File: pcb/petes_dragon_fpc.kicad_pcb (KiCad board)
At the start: 2 copper layers, 154.6 x 140.5 mm, 200 parts

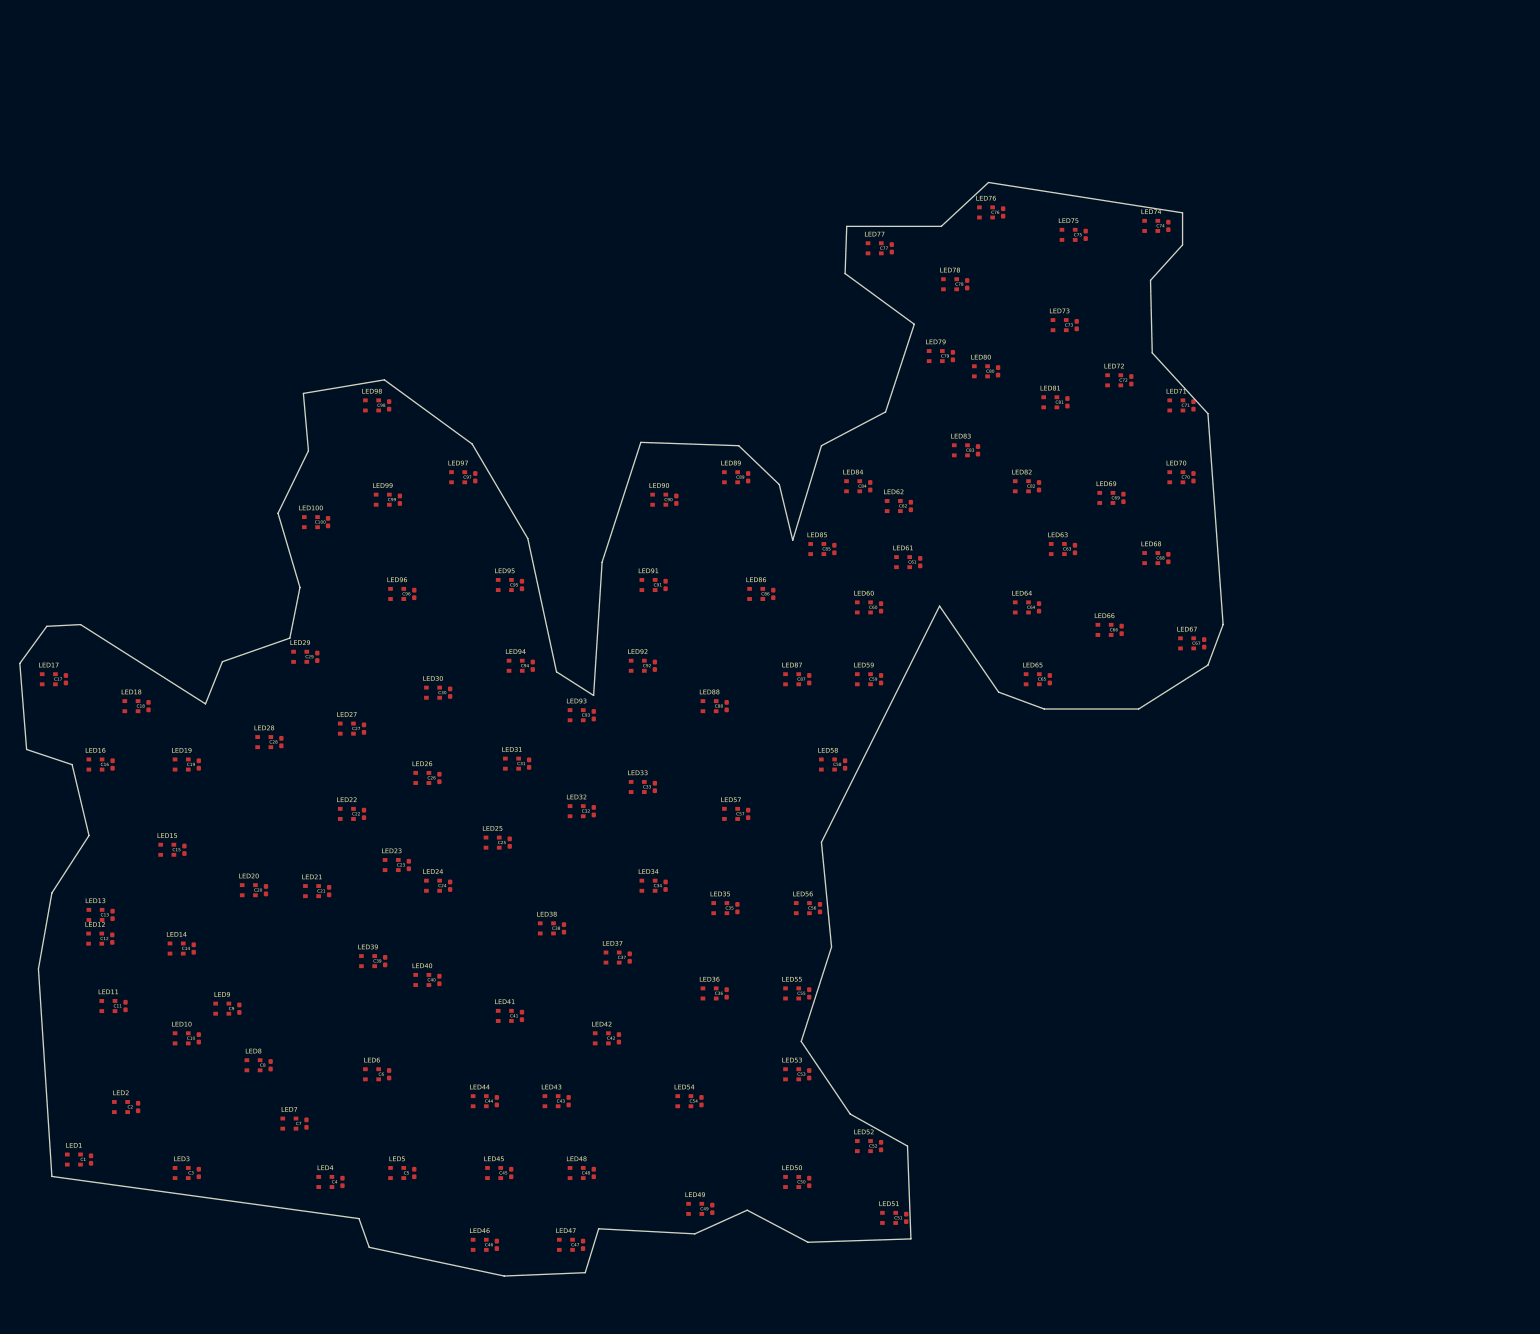
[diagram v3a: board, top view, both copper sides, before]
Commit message: feat(pcb): package KiCad project as zip with tracks for EasyEDA import
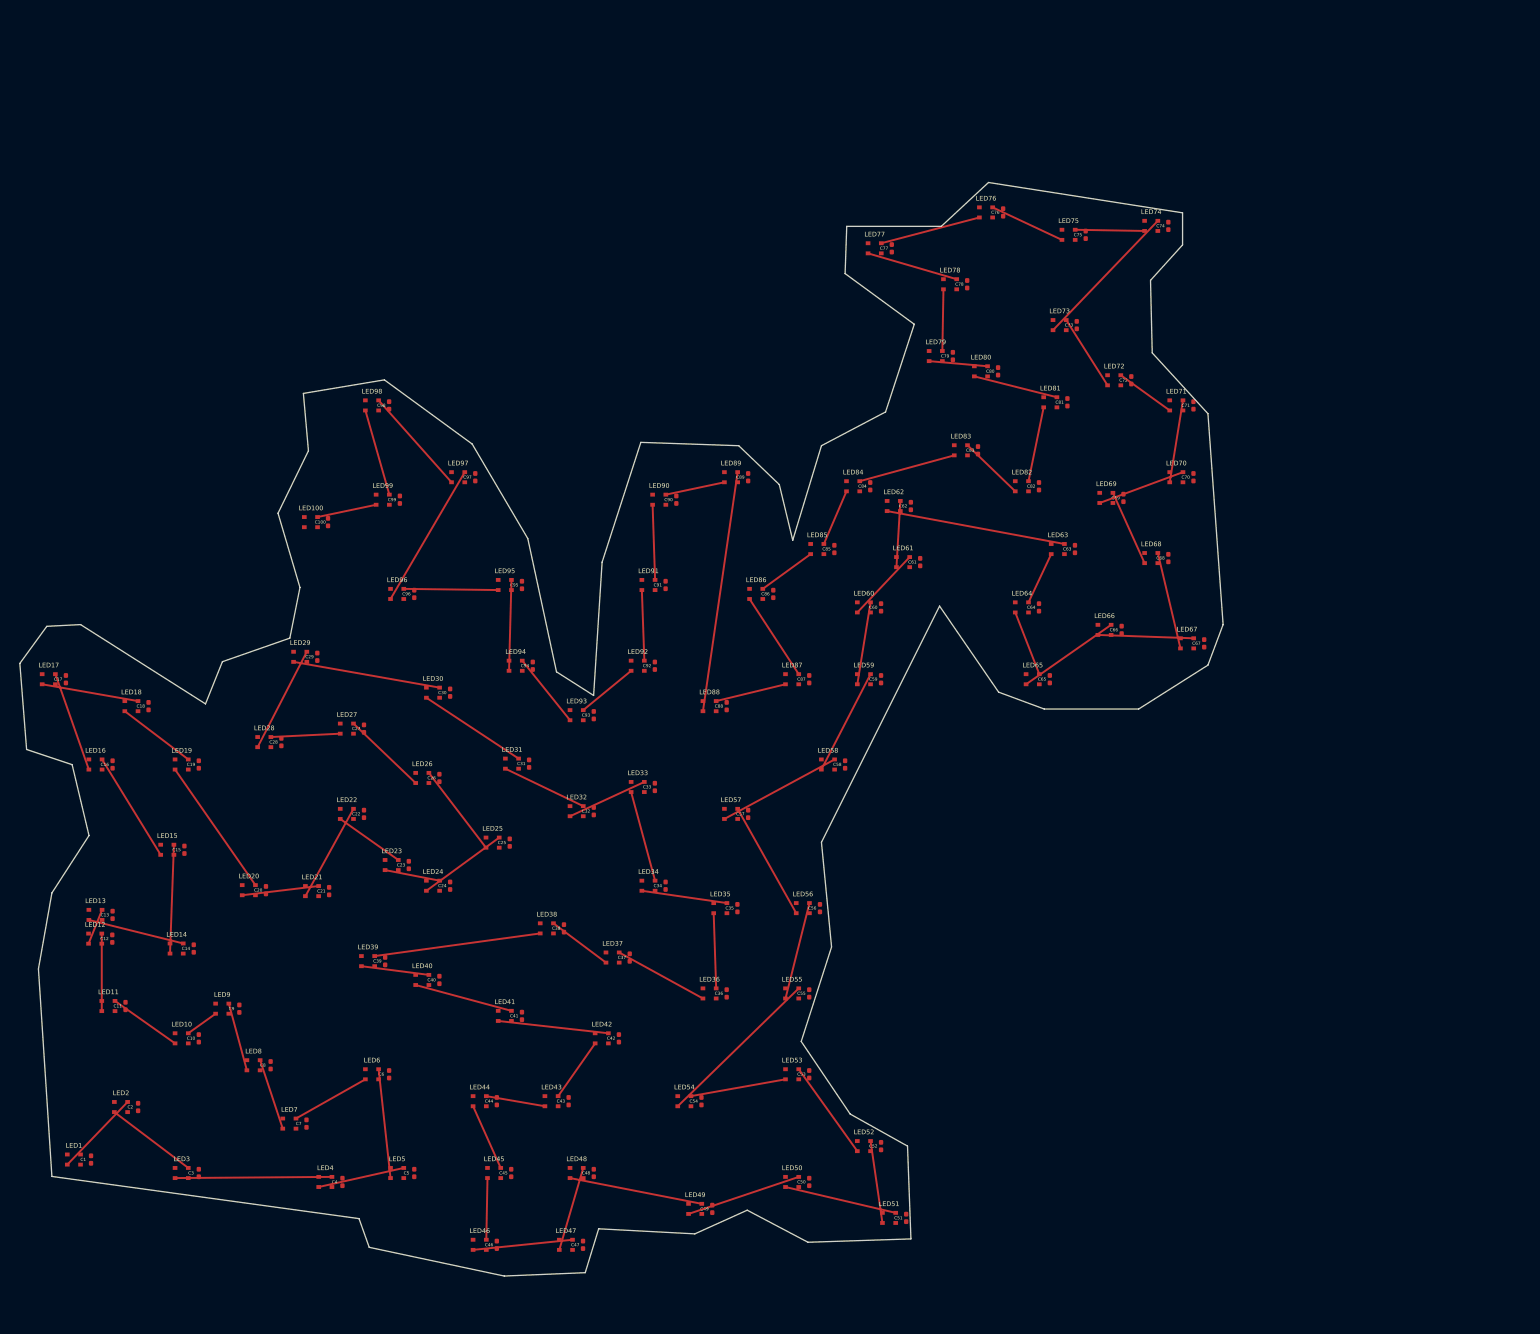
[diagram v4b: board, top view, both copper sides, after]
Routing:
- net DATA_89: track 0.00 -> 31.0 mm
- net DATA_63: track 0.00 -> 23.2 mm
- net DATA_55: track 0.00 -> 21.7 mm
- net DATA_39: track 0.00 -> 21.5 mm
- net DATA_4: track 0.00 -> 20.2 mm
- net DATA_74: track 0.00 -> 19.5 mm
- net DATA_30: track 0.00 -> 19.1 mm
- net DATA_97: track 0.00 -> 18.9 mm
- net DATA_20: track 0.00 -> 18.1 mm
- net DATA_49: track 0.00 -> 17.3 mm
- net DATA_58: track 0.00 -> 16.1 mm
- net DATA_57: track 0.00 -> 15.4 mm
- net DATA_50: track 0.00 -> 14.9 mm
- net DATA_51: track 0.00 -> 14.5 mm
- net DATA_16: track 0.00 -> 14.4 mm
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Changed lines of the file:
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@@
     (pad "2" smd roundrect (at 0.48 0) (size 0.56 0.62) (layers "F.Cu" "F.Paste" "F.Mask") (roundrect_rratio 0.25) (net 2 "GND"))
   )
+  (segment (start 17.81 170.25) (end 25.56 162.2) (width 0.25) (layer "F.Cu") (net 4))
+  (segment (start 23.86 163.5) (end 33.36 170.68) (width 0.25) (layer "F.Cu") (net 5))
+  (segment (start 31.66 171.98) (end 51.82 171.83) (width 0.25) (layer "F.Cu") (net 6))
+  (segment (start 50.12 173.13) (end 61.05 170.68) (width 0.25) (layer "F.Cu") (net 7))
+  (segment (start 59.35 171.98) (end 57.82 157.99) (width 0.25) (layer "F.Cu") (net 8))
+  (segment (start 56.12 159.29) (end 47.2 164.33) (width 0.25) (layer "F.Cu") (net 9))
+  (segment (start 45.5 165.63) (end 42.59 156.83) (width 0.25) (layer "F.Cu") (net 10))
+  (segment (start 40.89 158.13) (end 38.57 149.56) (width 0.25) (layer "F.Cu") (net 11))
+  (segment (start 36.87 150.86) (end 33.36 153.37) (width 0.25) (layer "F.Cu") (net 12))
+  (segment (start 31.66 154.67) (end 23.94 149.22) (width 0.25) (layer "F.Cu") (net 13))
+  (segment (start 22.24 150.52) (end 22.24 140.56) (width 0.25) (layer "F.Cu") (net 14))
+  (segment (start 20.54 141.86) (end 22.28 137.51) (width 0.25) (layer "F.Cu") (net 15))
+  (segment (start 20.58 138.81) (end 32.71 141.83) (width 0.25) (layer "F.Cu") (net 16))
+  (segment (start 31.01 143.13) (end 31.51 129.14) (width 0.25) (layer "F.Cu") (net 17))
+  (segment (start 29.81 130.44) (end 22.28 118.18) (width 0.25) (layer "F.Cu") (net 18))
+  (segment (start 20.58 119.48) (end 16.28 107.22) (width 0.25) (layer "F.Cu") (net 19))
+  (segment (start 14.58 108.52) (end 26.9 110.68) (width 0.25) (layer "F.Cu") (net 20))
+  (segment (start 25.2 111.98) (end 33.36 118.18) (width 0.25) (layer "F.Cu") (net 21))
+  (segment (start 31.66 119.48) (end 41.99 134.33) (width 0.25) (layer "F.Cu") (net 22))
+  (segment (start 40.29 135.63) (end 50.11 134.45) (width 0.25) (layer "F.Cu") (net 23))
+  (segment (start 48.41 135.75) (end 54.59 124.53) (width 0.25) (layer "F.Cu") (net 24))
+  (segment (start 52.89 125.83) (end 60.35 131.1) (width 0.25) (layer "F.Cu") (net 25))
+  (segment (start 58.65 132.4) (end 65.66 133.76) (width 0.25) (layer "F.Cu") (net 26))
+  (segment (start 63.96 135.06) (end 73.32 128.22) (width 0.25) (layer "F.Cu") (net 27))
+  (segment (start 71.62 129.52) (end 64.28 119.91) (width 0.25) (layer "F.Cu") (net 28))
+  (segment (start 62.58 121.21) (end 54.59 113.57) (width 0.25) (layer "F.Cu") (net 29))
+  (segment (start 52.89 114.87) (end 43.97 115.3) (width 0.25) (layer "F.Cu") (net 30))
+  (segment (start 42.27 116.6) (end 48.59 104.34) (width 0.25) (layer "F.Cu") (net 31))
+  (segment (start 46.89 105.64) (end 65.66 108.95) (width 0.25) (layer "F.Cu") (net 32))
+  (segment (start 63.96 110.25) (end 75.81 118.07) (width 0.25) (layer "F.Cu") (net 33))
+  (segment (start 74.11 119.37) (end 84.12 124.18) (width 0.25) (layer "F.Cu") (net 34))
+  (segment (start 82.42 125.48) (end 91.97 121.07) (width 0.25) (layer "F.Cu") (net 35))
+  (segment (start 90.27 122.37) (end 93.35 133.76) (width 0.25) (layer "F.Cu") (net 36))
+  (segment (start 91.65 135.06) (end 102.58 136.64) (width 0.25) (layer "F.Cu") (net 37))
+  (segment (start 100.88 137.94) (end 101.2 147.6) (width 0.25) (layer "F.Cu") (net 38))
+  (segment (start 99.5 148.9) (end 88.74 142.99) (width 0.25) (layer "F.Cu") (net 39))
+  (segment (start 87.04 144.29) (end 80.29 139.24) (width 0.25) (layer "F.Cu") (net 40))
+  (segment (start 78.59 140.54) (end 57.31 143.45) (width 0.25) (layer "F.Cu") (net 41))
+  (segment (start 55.61 144.75) (end 64.28 145.87) (width 0.25) (layer "F.Cu") (net 42))
+  (segment (start 62.58 147.17) (end 74.89 150.49) (width 0.25) (layer "F.Cu") (net 43))
+  (segment (start 73.19 151.79) (end 87.35 153.37) (width 0.25) (layer "F.Cu") (net 44))
+  (segment (start 85.65 154.67) (end 80.89 161.45) (width 0.25) (layer "F.Cu") (net 45))
+  (segment (start 79.19 162.75) (end 71.66 161.45) (width 0.25) (layer "F.Cu") (net 46))
+  (segment (start 69.96 162.75) (end 73.51 170.68) (width 0.25) (layer "F.Cu") (net 47))
+  (segment (start 71.81 171.98) (end 71.66 179.91) (width 0.25) (layer "F.Cu") (net 48))
+  (segment (start 69.96 181.21) (end 82.74 179.91) (width 0.25) (layer "F.Cu") (net 49))
+  (segment (start 81.04 181.21) (end 84.12 170.68) (width 0.25) (layer "F.Cu") (net 50))
+  (segment (start 82.42 171.98) (end 99.35 175.29) (width 0.25) (layer "F.Cu") (net 51))
+  (segment (start 97.65 176.59) (end 111.81 171.83) (width 0.25) (layer "F.Cu") (net 52))
+  (segment (start 110.11 173.13) (end 124.27 176.45) (width 0.25) (layer "F.Cu") (net 53))
+  (segment (start 122.57 177.75) (end 121.04 167.22) (width 0.25) (layer "F.Cu") (net 54))
+  (segment (start 119.34 168.52) (end 111.81 157.99) (width 0.25) (layer "F.Cu") (net 55))
+  (segment (start 110.11 159.29) (end 97.96 161.45) (width 0.25) (layer "F.Cu") (net 56))
+  (segment (start 96.26 162.75) (end 111.81 147.6) (width 0.25) (layer "F.Cu") (net 57))
+  (segment (start 110.11 148.9) (end 113.19 136.64) (width 0.25) (layer "F.Cu") (net 58))
+  (segment (start 111.49 137.94) (end 103.96 124.53) (width 0.25) (layer "F.Cu") (net 59))
+  (segment (start 102.26 125.83) (end 116.42 118.18) (width 0.25) (layer "F.Cu") (net 60))
+  (segment (start 114.72 119.48) (end 121.04 107.22) (width 0.25) (layer "F.Cu") (net 61))
+  (segment (start 119.34 108.52) (end 121.04 97.99) (width 0.25) (layer "F.Cu") (net 62))
+  (segment (start 119.34 99.29) (end 126.07 92.17) (width 0.25) (layer "F.Cu") (net 63))
+  (segment (start 124.37 93.47) (end 124.87 84.96) (width 0.25) (layer "F.Cu") (net 64))
+  (segment (start 123.17 86.26) (end 145.96 90.49) (width 0.25) (layer "F.Cu") (net 65))
+  (segment (start 144.26 91.79) (end 141.34 97.99) (width 0.25) (layer "F.Cu") (net 66))
+  (segment (start 139.64 99.29) (end 142.73 107.22) (width 0.25) (layer "F.Cu") (net 67))
+  (segment (start 141.03 108.52) (end 151.96 100.88) (width 0.25) (layer "F.Cu") (net 68))
+  (segment (start 150.26 102.18) (end 162.57 102.61) (width 0.25) (layer "F.Cu") (net 69))
+  (segment (start 160.87 103.91) (end 157.96 91.65) (width 0.25) (layer "F.Cu") (net 70))
+  (segment (start 156.26 92.95) (end 152.19 83.92) (width 0.25) (layer "F.Cu") (net 71))
+  (segment (start 150.49 85.22) (end 161.19 81.26) (width 0.25) (layer "F.Cu") (net 72))
+  (segment (start 159.49 82.56) (end 161.19 72.03) (width 0.25) (layer "F.Cu") (net 73))
+  (segment (start 159.49 73.33) (end 153.2 68.8) (width 0.25) (layer "F.Cu") (net 74))
+  (segment (start 151.5 70.1) (end 146.19 61.71) (width 0.25) (layer "F.Cu") (net 75))
+  (segment (start 144.49 63.01) (end 157.96 48.96) (width 0.25) (layer "F.Cu") (net 76))
+  (segment (start 156.26 50.26) (end 147.34 50.11) (width 0.25) (layer "F.Cu") (net 77))
+  (segment (start 145.64 51.41) (end 136.73 47.23) (width 0.25) (layer "F.Cu") (net 78))
+  (segment (start 135.03 48.53) (end 122.42 51.84) (width 0.25) (layer "F.Cu") (net 79))
+  (segment (start 120.72 53.14) (end 132.11 56.46) (width 0.25) (layer "F.Cu") (net 80))
+  (segment (start 130.41 57.76) (end 130.27 65.69) (width 0.25) (layer "F.Cu") (net 81))
+  (segment (start 128.57 66.99) (end 136.08 67.65) (width 0.25) (layer "F.Cu") (net 82))
+  (segment (start 134.38 68.95) (end 144.99 71.63) (width 0.25) (layer "F.Cu") (net 83))
+  (segment (start 143.29 72.93) (end 141.34 82.42) (width 0.25) (layer "F.Cu") (net 84))
+  (segment (start 139.64 83.72) (end 133.5 77.8) (width 0.25) (layer "F.Cu") (net 85))
+  (segment (start 131.8 79.1) (end 119.65 82.42) (width 0.25) (layer "F.Cu") (net 86))
+  (segment (start 117.95 83.72) (end 115.04 90.49) (width 0.25) (layer "F.Cu") (net 87))
+  (segment (start 113.34 91.79) (end 107.19 96.26) (width 0.25) (layer "F.Cu") (net 88))
+  (segment (start 105.49 97.56) (end 111.81 107.22) (width 0.25) (layer "F.Cu") (net 89))
+  (segment (start 110.11 108.52) (end 101.2 110.68) (width 0.25) (layer "F.Cu") (net 90))
+  (segment (start 99.5 111.98) (end 103.96 81.26) (width 0.25) (layer "F.Cu") (net 91))
+  (segment (start 102.26 82.56) (end 94.73 84.15) (width 0.25) (layer "F.Cu") (net 92))
+  (segment (start 93.03 85.45) (end 93.35 95.11) (width 0.25) (layer "F.Cu") (net 93))
+  (segment (start 91.65 96.41) (end 91.97 105.49) (width 0.25) (layer "F.Cu") (net 94))
+  (segment (start 90.27 106.79) (end 84.12 111.84) (width 0.25) (layer "F.Cu") (net 95))
+  (segment (start 82.42 113.14) (end 76.28 105.49) (width 0.25) (layer "F.Cu") (net 96))
+  (segment (start 74.58 106.79) (end 74.89 95.11) (width 0.25) (layer "F.Cu") (net 97))
+  (segment (start 73.19 96.41) (end 61.05 96.26) (width 0.25) (layer "F.Cu") (net 98))
+  (segment (start 59.35 97.56) (end 68.89 81.26) (width 0.25) (layer "F.Cu") (net 99))
+  (segment (start 67.19 82.56) (end 57.82 72.03) (width 0.25) (layer "F.Cu") (net 100))
+  (segment (start 56.12 73.33) (end 59.2 84.15) (width 0.25) (layer "F.Cu") (net 101))
+  (segment (start 57.5 85.45) (end 49.97 87.03) (width 0.25) (layer "F.Cu") (net 102))
 )

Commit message: fix(pcb): format kicad_pcb with KiCad 5 module syntax for EasyEDA Standard compatibility
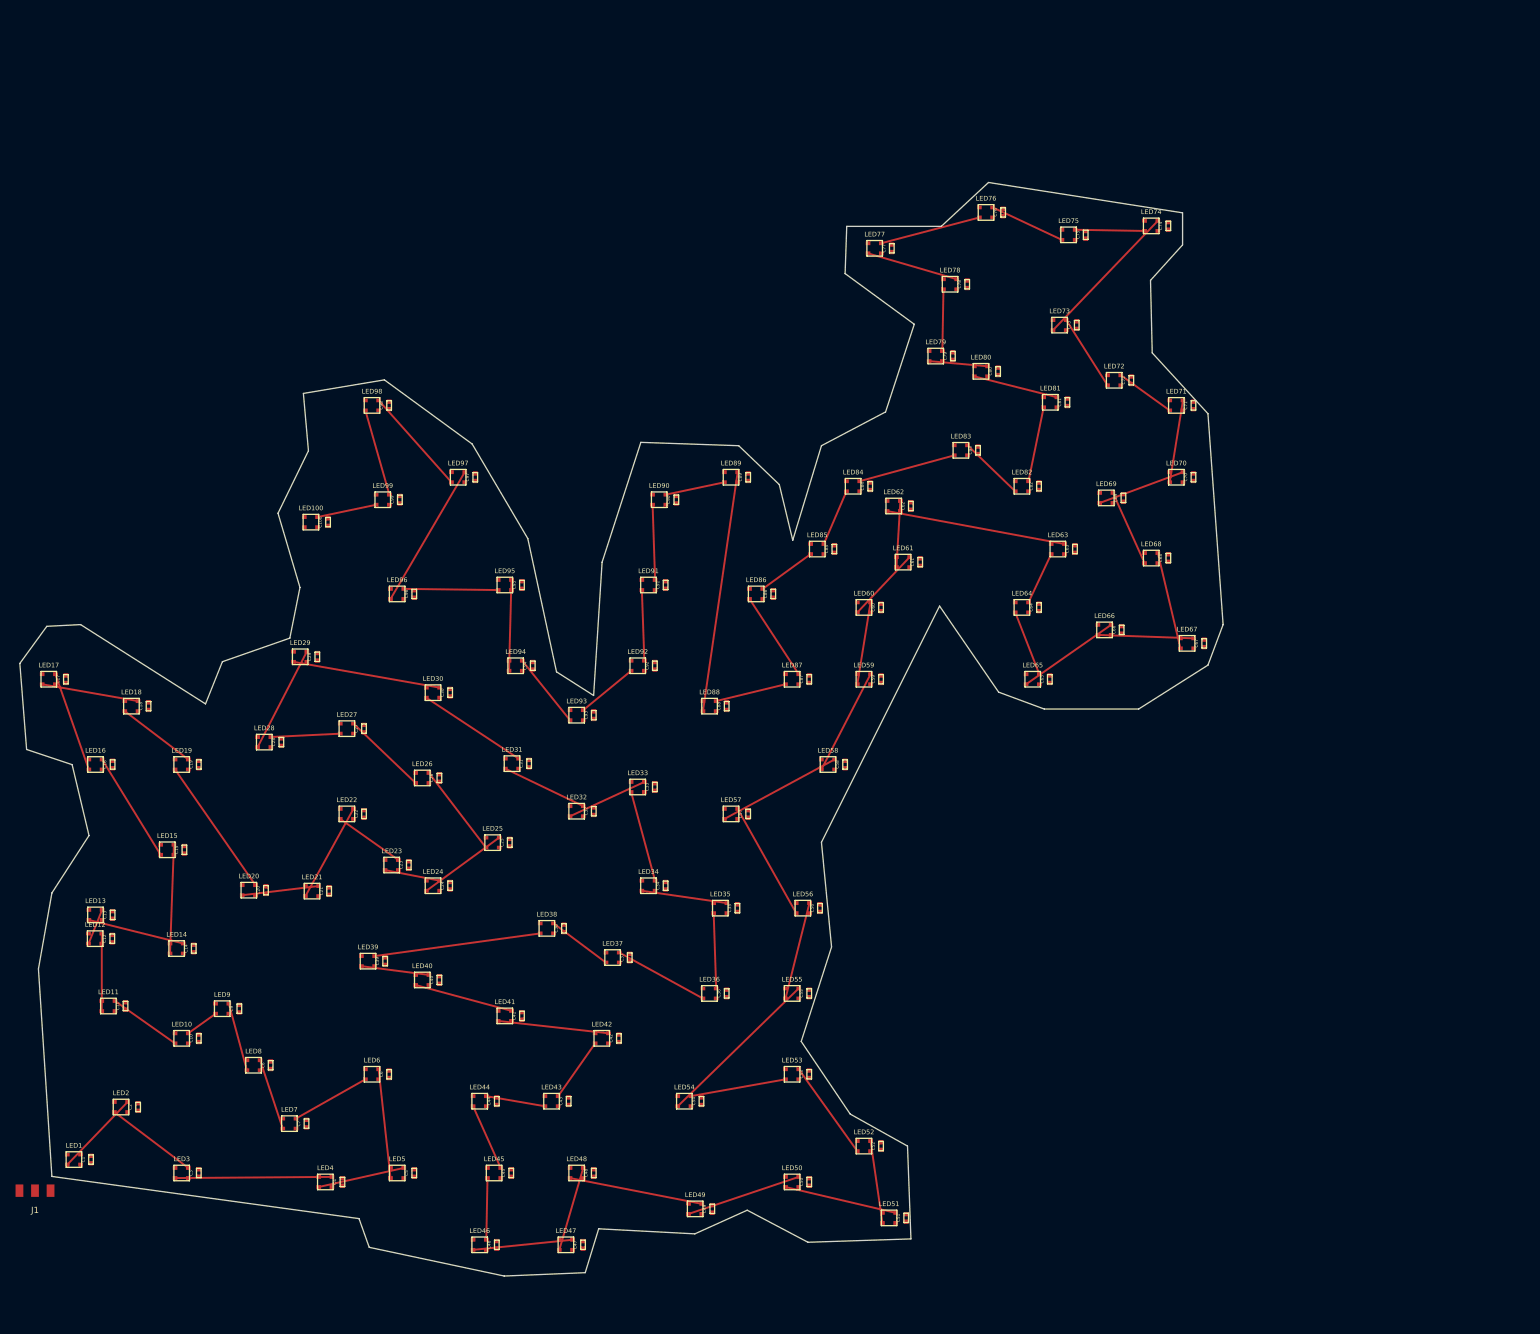
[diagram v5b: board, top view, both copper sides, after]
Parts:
- added J1: JST-PH-3P, Connector_JST:JST_PH_S3B-PH-SM4-TB_1x03-1MP_P2.00mm_Horizontal, F.Cu at (13.7, 173.6)
